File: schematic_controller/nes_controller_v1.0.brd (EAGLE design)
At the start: 110.2 x 55.9 mm, 23 parts

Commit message: updated schematic with debounced buttons
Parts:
- added C1, C2, C3, C4, C5, C6, C7, C8: (no value), rcl:C0805K
- added R10, R11, R12, R13, R14, R15, R16, R17: (no value), rcl:MINI_MELF-0207R
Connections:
- new net 3§4: C2.1, R12.2, R2.2, SELECT.1
- new net 4$5: A.1, C3.1, R11.2, R3.2
- new net N$3: C1.1, R1.2, R10.2, START.1
- new net N$4: B.1, C4.1, R14.2, R4.2
- new net N$5: C5.1, R13.2, R5.2, UP.1
- new net N$6: C6.1, DOWN.1, R15.2, R6.2
- new net N$7: C7.1, R16.2, R7.2, RIGHT.1
- new net N$8: C8.1, LEFT.1, R17.2, R8.2
- net A: now also R11.1; no longer A.1, R3.2
- net B: now also R14.1; no longer B.1, R4.2
- net DOWN: now also R15.1; no longer DOWN.1, R6.2
- net GND: now also C1.2, C2.2, C3.2, C4.2, C5.2, C6.2, C7.2, C8.2
- net LEFT: now also R17.1; no longer LEFT.1, R8.2
- net RIGHT: now also R16.1; no longer R7.2, RIGHT.1
- net SELECT: now also R12.1; no longer R2.2, SELECT.1
- net START: now also R10.1; no longer R1.2, START.1
- net UP: now also R13.1; no longer R5.2, UP.1
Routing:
- net SELECT: track 95.2 -> 48.6 mm
- net LEFT: track 126.9 -> 82.9 mm
- net DOWN: track 138.9 -> 96.3 mm
- net 3§4: track 0.00 -> 37.9 mm
- net RIGHT: track 95.4 -> 64.5 mm
- net UP: track 89.5 -> 71.2 mm
- net B: track 113.6 -> 105.8 mm
- net START: track 101.7 -> 95.8 mm
- net A: track 114.3 -> 109.7 mm

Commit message: finished board layout
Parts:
- removed U$1: (no value), HTL-Logo:LOGO_8
- moved C4 130.9 mm to (83.7, 2.44)
- moved C7 124.9 mm to (35.4, 17.1), turned to 90 degrees
- moved R14 120.8 mm to (76.8, 2.44)
- moved C3 120.3 mm to (88.2, 9.35), turned to 90 degrees
- moved R16 116.9 mm to (31.7, 17.5), turned to 270 degrees
- moved R11 110.6 mm to (91.8, 9.35), turned to 270 degrees
- moved R17 109.9 mm to (3.25, 24.0), turned to 270 degrees
- moved C8 105.8 mm to (2.84, 10.2), turned to 270 degrees
- moved C5 93.5 mm to (8.53, 27.2), turned to 90 degrees
- moved R13 89.0 mm to (11.8, 27.2), turned to 270 degrees
- moved C6 88.6 mm to (8.94, 7.32), turned to 270 degrees
- moved R15 85.6 mm to (12.6, 7.32), turned to 90 degrees
- moved C2 74.6 mm to (39.4, 10.2), turned to 90 degrees
- moved R12 72.7 mm to (42.7, 10.2), turned to 270 degrees
- moved C1 70.6 mm to (54.5, 10.2), turned to 270 degrees
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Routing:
- net GND: track 217.6 -> 425.5 mm, vias 6 -> 4
- net +3V3: track 263.9 -> 359.7 mm, vias 1 -> 7
- net 4$5: track 0.00 -> 77.0 mm
- net A: track 109.7 -> 35.5 mm, vias 2 -> 0
- net N$4: track 0.00 -> 69.8 mm
- net N$3: track 0.00 -> 42.9 mm
- net SELECT: track 48.6 -> 89.4 mm
- net N$6: track 0.00 -> 38.0 mm
- net N$7: track 0.00 -> 36.8 mm
- net N$8: track 0.00 -> 32.5 mm
- net B: track 105.8 -> 76.5 mm
- net N$5: track 0.00 -> 24.4 mm
- net START: track 95.8 -> 81.3 mm
- net RIGHT: track 64.5 -> 78.1 mm
- net UP: track 71.2 -> 76.4 mm
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
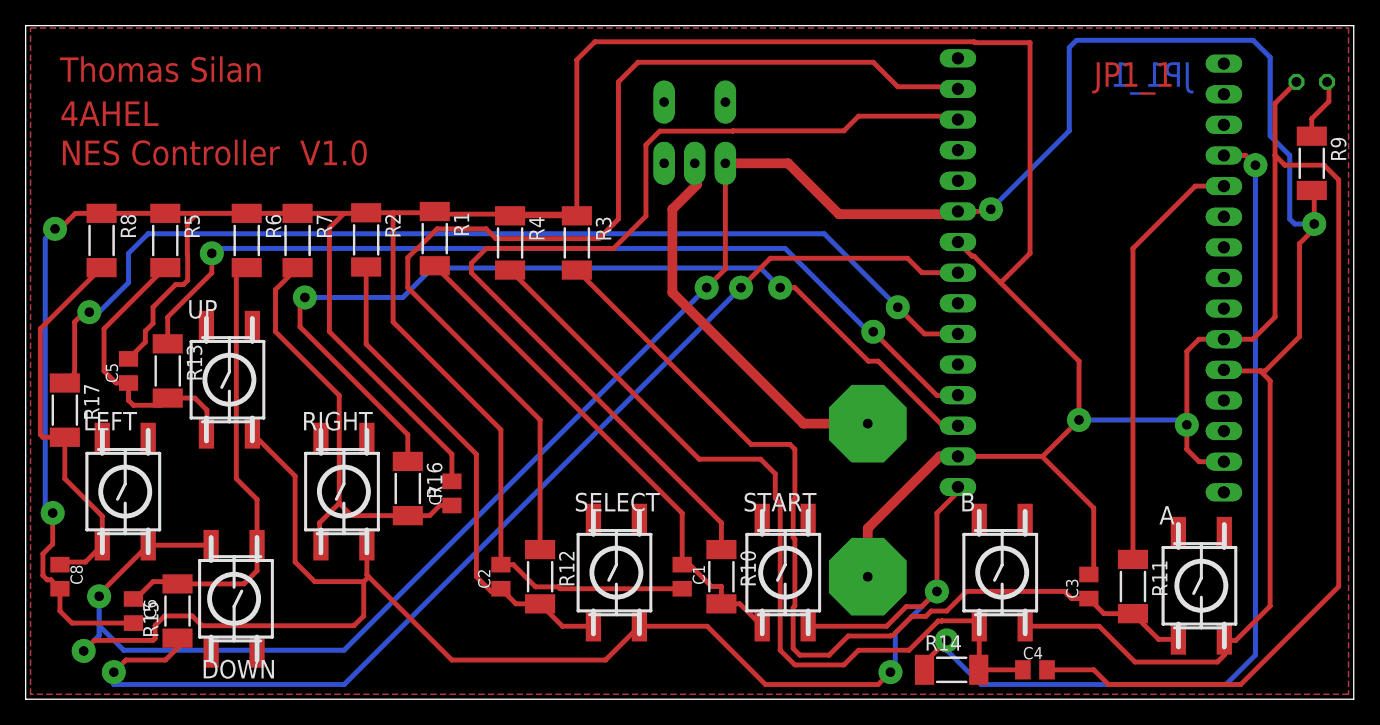
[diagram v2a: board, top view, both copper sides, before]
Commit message: changed bigger led hole
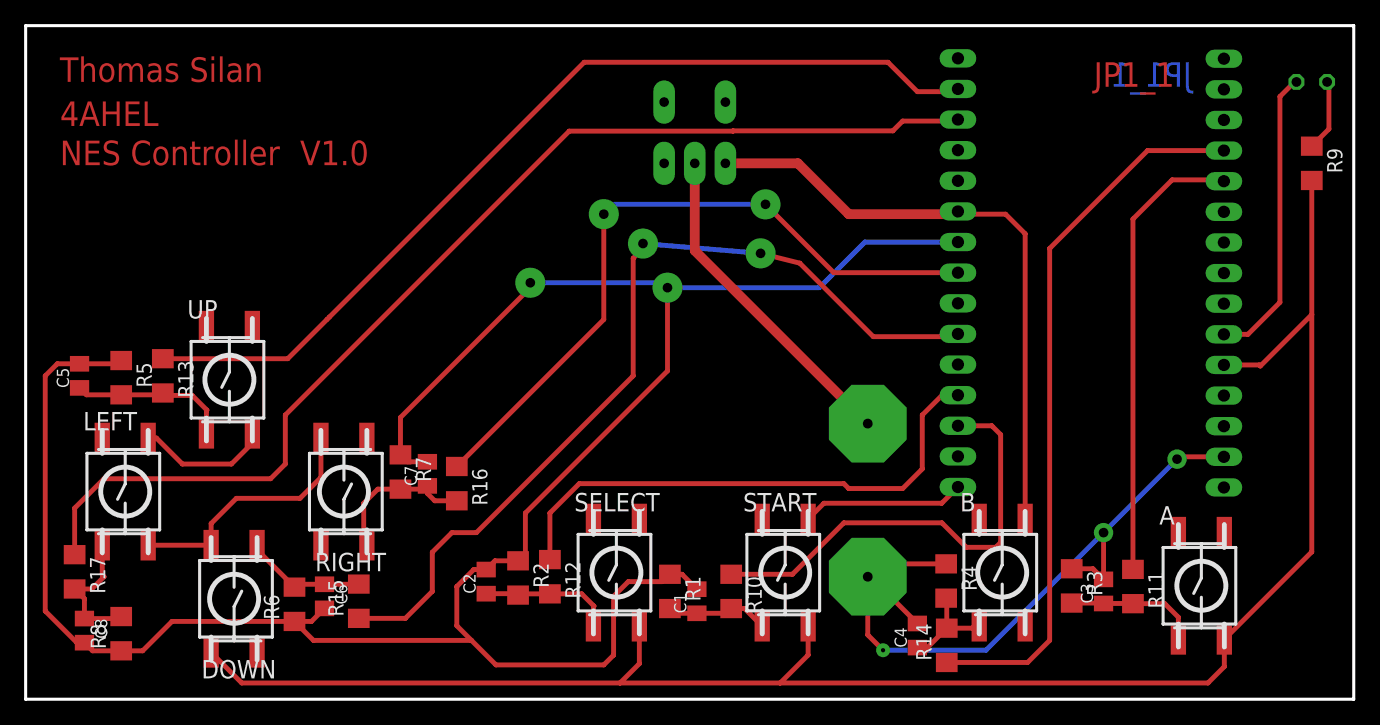
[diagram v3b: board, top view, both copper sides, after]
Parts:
- R1, R10, R11, R12, R13, R14, R15, R16, R17, R2, R3, R4, R5, R6, R7, R8, R9: device rcl:MINI_MELF-0207R -> rcl:R1206
- moved R3 49.9 mm to (86.8, 9.40)
- moved R4 45.8 mm to (76.4, 9.80)
- moved R1 35.2 mm to (53.4, 8.94)
- moved R8 32.7 mm to (7.92, 5.44), turned to 90 degrees
- moved R2 30.7 mm to (40.8, 10.1)
- moved R6 30.4 mm to (22.3, 7.87), turned to 90 degrees
- moved R7 21.0 mm to (31.1, 18.8)
- moved C6 15.9 mm to (24.8, 8.53)
- moved R15 15.1 mm to (27.6, 8.13)
- moved R17 13.4 mm to (4.06, 10.6)
- moved R5 12.0 mm to (7.92, 26.7)
- moved C4 10.2 mm to (74.0, 5.28), turned to 90 degrees
- moved C8 4.91 mm to (4.88, 5.69)
- moved C5 4.08 mm to (4.47, 26.8)
- moved R16 4.08 mm to (35.8, 17.9)
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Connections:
- net +3V3: now also A.22, B.22, DOWN.22, LEFT.22, RIGHT.22, SELECT.22, START.22, UP.22
- net 3§4: now also SELECT.11
- net 4$5: now also A.11
- net DOWN: now also JP2.10; no longer JP2.8
- net LEFT: now also JP2.3; no longer JP2.10
- net N$3: now also START.11
- net N$4: now also B.11
- net N$5: now also UP.11
- net N$6: now also DOWN.11
- net N$7: now also RIGHT.11
- net N$8: now also LEFT.11
- net RIGHT: now also JP2.8; no longer JP2.13
- net SELECT: now also JP2.12; no longer JP2.2
- net START: now also JP2.13; no longer JP2.3
- net UP: now also JP2.2; no longer JP2.12
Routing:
- net GND: track 425.5 -> 276.3 mm, vias 4 -> 5
- net +3V3: track 359.7 -> 246.0 mm, vias 7 -> 0
- net 4$5: track 77.0 -> 11.2 mm
- net N$4: track 69.8 -> 9.28 mm
- net SELECT: track 89.4 -> 44.7 mm
- net START: track 81.3 -> 37.9 mm
- net N$3: track 42.9 -> 8.58 mm
- net 3§4: track 41.1 -> 11.2 mm
- net N$6: track 38.0 -> 10.2 mm
- net N$7: track 36.8 -> 12.8 mm
- net N$8: track 32.5 -> 11.4 mm
- net DOWN: track 94.0 -> 73.2 mm
- net RIGHT: track 78.1 -> 58.0 mm
- net B: track 76.5 -> 59.6 mm, vias 2 -> 0
- net N$5: track 24.4 -> 13.4 mm
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- removed copper zone on layer 1, net GND
- removed copper zone on layer 16, net GND
